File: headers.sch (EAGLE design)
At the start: 15 parts

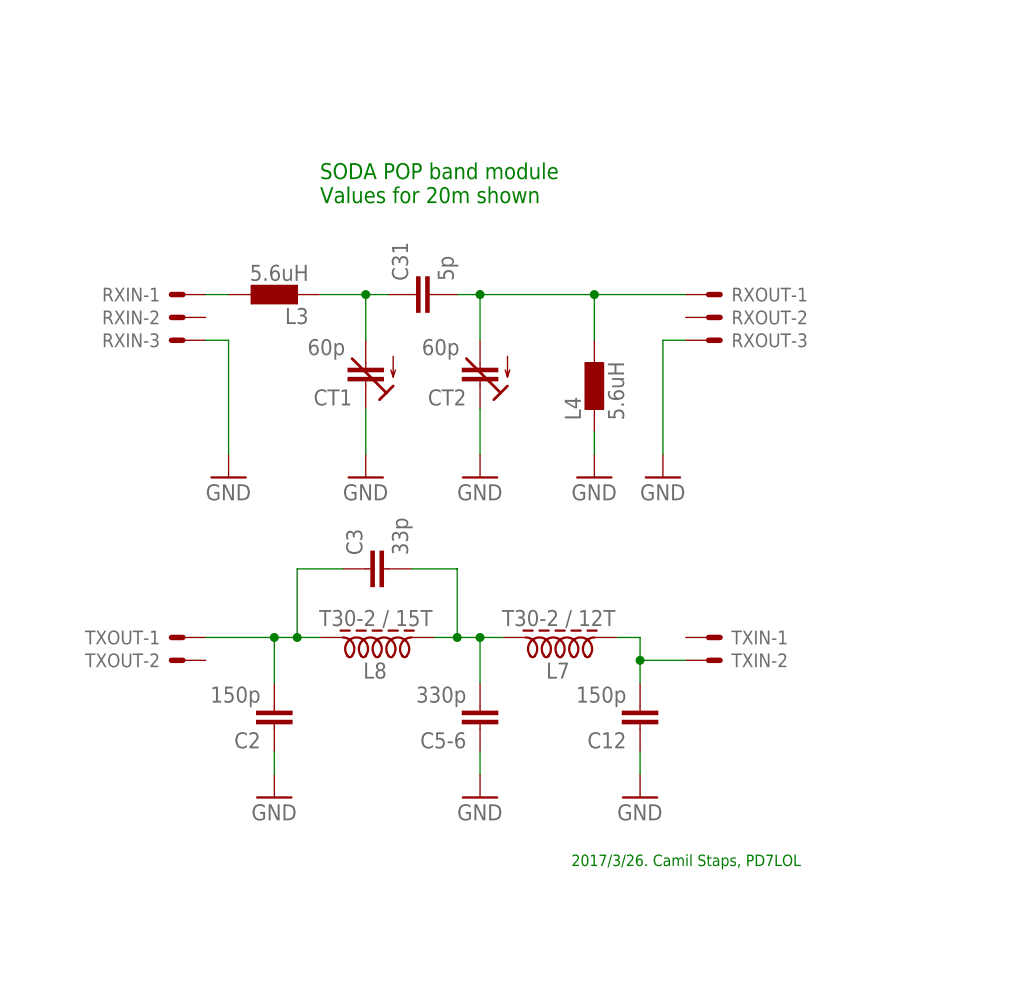
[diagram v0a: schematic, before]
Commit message: Headers: split C5-6 again, make some TX traces shorter
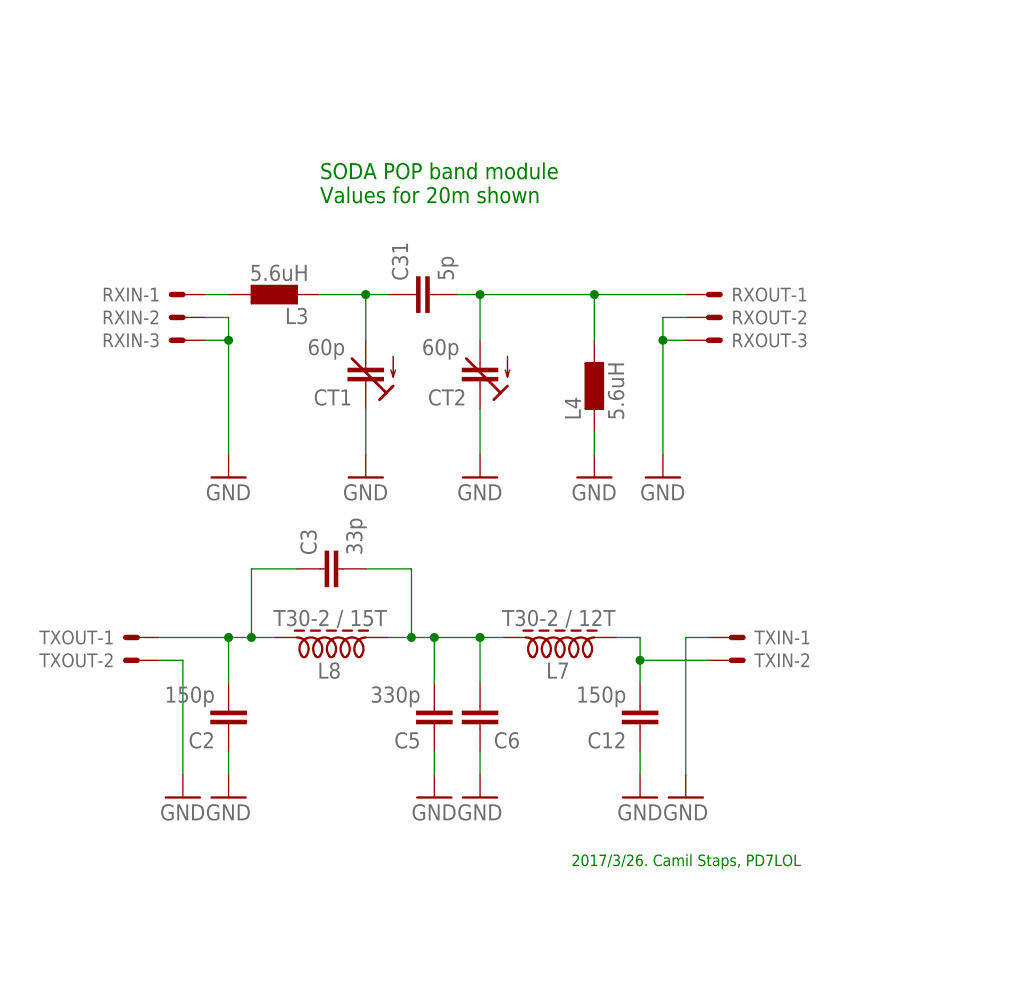
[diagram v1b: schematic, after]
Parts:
- added C5: 330p, capacitor-wima:C5/2.5
- renumbered C5-6 to C6
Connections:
- net GND: now also C5.1, RXIN-2.S, RXOUT-2.S, TXIN-1.S, TXOUT-2.S
- net N$5: now also C5.2
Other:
- moved on the sheet: C2, C3, L8, TXIN-1, TXIN-2, TXOUT-1, TXOUT-2
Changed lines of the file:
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@@
 <part name="L8" library="toroids" deviceset="INDUCTOR" device="T30-2-28AWG-15T" value="T30-2 / 15T"/>
 <part name="L7" library="toroids" deviceset="INDUCTOR" device="T30-2-28AWG-15T" value="T30-2 / 12T"/>
-<part name="C5-6" library="capacitor-wima" deviceset="C" device="5/2.5" value="330p"/>
+<part name="C5" library="capacitor-wima" deviceset="C" device="5/2.5" value="330p"/>
 <part name="C12" library="capacitor-wima" deviceset="C" device="5/2.5" value="150p"/>
 <part name="C3" library="capacitor-wima" deviceset="C" device="5/2.5" value="33p"/>
@@
 <part name="L4" library="eagle-ltspice" deviceset="L" device="0207/10" value="5.6uH"/>
 <part name="L3" library="eagle-ltspice" deviceset="L" device="0207/10" value="5.6uH"/>
+<part name="C6" library="capacitor-wima" deviceset="C" device="5/2.5" value="330p"/>
+<part name="GND9" library="supply1" deviceset="GND" device=""/>
+<part name="GND10" library="supply1" deviceset="GND" device=""/>
+<part name="GND11" library="supply1" deviceset="GND" device=""/>
 </parts>
 <sheets>
@@
 <instance part="GND4" gate="1" x="48.26" y="45.72"/>
 <instance part="GND5" gate="1" x="60.96" y="45.72"/>
-<instance part="TXIN" gate="-1" x="73.66" y="27.94" smashed="yes">
-<attribute name="NAME" x="76.2" y="27.178" size="1.524" layer="95"/>
-</instance>
-<instance part="TXIN" gate="-2" x="73.66" y="25.4"/>
-<instance part="TXOUT" gate="-1" x="15.24" y="27.94" smashed="yes" rot="MR0">
-<attribute name="NAME" x="12.7" y="27.178" size="1.524" layer="95" rot="MR0"/>
-</instance>
-<instance part="TXOUT" gate="-2" x="15.24" y="25.4" rot="MR0"/>
-<instance part="C2" gate="G$1" x="25.4" y="17.78" rot="R180"/>
-<instance part="L8" gate="G$1" x="38.1" y="27.94" smashed="yes" rot="R180">
-<attribute name="NAME" x="37.9" y="25.146" size="1.778" layer="95" rot="R180"/>
-<attribute name="VALUE" x="42.98" y="30.988" size="1.778" layer="96" rot="R180"/>
+<instance part="TXIN" gate="-1" x="76.2" y="27.94" smashed="yes">
+<attribute name="NAME" x="78.74" y="27.178" size="1.524" layer="95"/>
+</instance>
+<instance part="TXIN" gate="-2" x="76.2" y="25.4"/>
+<instance part="TXOUT" gate="-1" x="10.16" y="27.94" smashed="yes" rot="MR0">
+<attribute name="NAME" x="7.62" y="27.178" size="1.524" layer="95" rot="MR0"/>
+</instance>
+<instance part="TXOUT" gate="-2" x="10.16" y="25.4" rot="MR0"/>
+<instance part="C2" gate="G$1" x="20.32" y="17.78" rot="R180"/>
+<instance part="L8" gate="G$1" x="33.02" y="27.94" smashed="yes" rot="R180">
+<attribute name="NAME" x="32.82" y="25.146" size="1.778" layer="95" rot="R180"/>
+<attribute name="VALUE" x="37.9" y="30.988" size="1.778" layer="96" rot="R180"/>
 </instance>
 <instance part="L7" gate="G$1" x="58.42" y="27.94" smashed="yes" rot="R180">
@@
 <attribute name="VALUE" x="63.3" y="30.988" size="1.778" layer="96" rot="R180"/>
 </instance>
-<instance part="C5-6" gate="G$1" x="48.26" y="17.78" smashed="yes" rot="R180">
-<attribute name="NAME" x="46.736" y="17.399" size="1.778" layer="95" rot="R180"/>
-<attribute name="VALUE" x="46.736" y="22.479" size="1.778" layer="96" rot="R180"/>
+<instance part="C5" gate="G$1" x="43.18" y="17.78" smashed="yes" rot="R180">
+<attribute name="NAME" x="41.656" y="17.399" size="1.778" layer="95" rot="R180"/>
+<attribute name="VALUE" x="41.656" y="22.479" size="1.778" layer="96" rot="R180"/>
 </instance>
 <instance part="C12" gate="G$1" x="66.04" y="17.78" rot="R180"/>
-<instance part="C3" gate="G$1" x="35.56" y="35.56" rot="R90"/>
-<instance part="GND6" gate="1" x="25.4" y="10.16"/>
-<instance part="GND7" gate="1" x="48.26" y="10.16"/>
+<instance part="C3" gate="G$1" x="30.48" y="35.56" rot="R90"/>
+<instance part="GND6" gate="1" x="20.32" y="10.16"/>
+<instance part="GND7" gate="1" x="43.18" y="10.16"/>
 <instance part="GND8" gate="1" x="66.04" y="10.16"/>
 <instance part="L4" gate="G$1" x="60.96" y="55.88"/>
 <instance part="L3" gate="G$1" x="25.4" y="66.04" rot="R90"/>
+<instance part="C6" gate="G$1" x="48.26" y="17.78" smashed="yes" rot="R180">
+<attribute name="NAME" x="49.784" y="15.621" size="1.778" layer="95"/>
+</instance>
+<instance part="GND9" gate="1" x="48.26" y="10.16"/>
+<instance part="GND10" gate="1" x="15.24" y="10.16"/>
+<instance part="GND11" gate="1" x="71.12" y="10.16"/>
 </instances>
 <busses>
@@
 <pinref part="RXOUT" gate="-3" pin="S"/>
 <wire x1="71.12" y1="60.96" x2="68.58" y2="60.96" width="0.1524" layer="91"/>
+<pinref part="RXOUT" gate="-2" pin="S"/>
+<wire x1="71.12" y1="63.5" x2="68.58" y2="63.5" width="0.1524" layer="91"/>
+<wire x1="68.58" y1="63.5" x2="68.58" y2="60.96" width="0.1524" layer="91"/>
+<junction x="68.58" y="60.96"/>
 </segment>
 <segment>
@@
 <wire x1="17.78" y1="60.96" x2="20.32" y2="60.96" width="0.1524" layer="91"/>
 <wire x1="20.32" y1="60.96" x2="20.32" y2="48.26" width="0.1524" layer="91"/>
+<pinref part="RXIN" gate="-2" pin="S"/>
+<wire x1="17.78" y1="63.5" x2="20.32" y2="63.5" width="0.1524" layer="91"/>
+<wire x1="20.32" y1="63.5" x2="20.32" y2="60.96" width="0.1524" layer="91"/>
+<junction x="20.32" y="60.96"/>
 </segment>
 <segment>
@@
 <pinref part="C2" gate="G$1" pin="1"/>
 <pinref part="GND6" gate="1" pin="GND"/>
-<wire x1="25.4" y1="15.24" x2="25.4" y2="12.7" width="0.1524" layer="91"/>
-</segment>
-<segment>
-<pinref part="C5-6" gate="G$1" pin="1"/>
+<wire x1="20.32" y1="15.24" x2="20.32" y2="12.7" width="0.1524" layer="91"/>
+</segment>
+<segment>
+<pinref part="C5" gate="G$1" pin="1"/>
 <pinref part="GND7" gate="1" pin="GND"/>
-<wire x1="48.26" y1="15.24" x2="48.26" y2="12.7" width="0.1524" layer="91"/>
+<wire x1="43.18" y1="15.24" x2="43.18" y2="12.7" width="0.1524" layer="91"/>
 </segment>
 <segment>
@@
 <pinref part="CT2" gate="G$1" pin="E"/>
 <wire x1="48.26" y1="48.26" x2="48.26" y2="53.34" width="0.1524" layer="91"/>
+</segment>
+<segment>
+<pinref part="GND9" gate="1" pin="GND"/>
+<pinref part="C6" gate="G$1" pin="1"/>
+<wire x1="48.26" y1="12.7" x2="48.26" y2="15.24" width="0.1524" layer="91"/>
+</segment>
+<segment>
+<pinref part="TXOUT" gate="-2" pin="S"/>
+<pinref part="GND10" gate="1" pin="GND"/>
+<wire x1="12.7" y1="25.4" x2="15.24" y2="25.4" width="0.1524" layer="91"/>
+<wire x1="15.24" y1="25.4" x2="15.24" y2="12.7" width="0.1524" layer="91"/>
+</segment>
+<segment>
+<pinref part="TXIN" gate="-1" pin="S"/>
+<pinref part="GND11" gate="1" pin="GND"/>
+<wire x1="73.66" y1="27.94" x2="71.12" y2="27.94" width="0.1524" layer="91"/>
+<wire x1="71.12" y1="27.94" x2="71.12" y2="12.7" width="0.1524" layer="91"/>
 </segment>
 </net>
@@
 <net name="N$5" class="0">
 <segment>
-<pinref part="C5-6" gate="G$1" pin="2"/>
-<wire x1="45.72" y1="27.94" x2="48.26" y2="27.94" width="0.1524" layer="91"/>
-<wire x1="48.26" y1="27.94" x2="48.26" y2="22.86" width="0.1524" layer="91"/>
+<pinref part="C5" gate="G$1" pin="2"/>
+<wire x1="40.64" y1="27.94" x2="43.18" y2="27.94" width="0.1524" layer="91"/>
+<wire x1="43.18" y1="27.94" x2="43.18" y2="22.86" width="0.1524" layer="91"/>
 <pinref part="C3" gate="G$1" pin="2"/>
-<wire x1="40.64" y1="35.56" x2="45.72" y2="35.56" width="0.1524" layer="91"/>
-<wire x1="45.72" y1="35.56" x2="45.72" y2="27.94" width="0.1524" layer="91"/>
+<wire x1="35.56" y1="35.56" x2="40.64" y2="35.56" width="0.1524" layer="91"/>
+<wire x1="40.64" y1="35.56" x2="40.64" y2="27.94" width="0.1524" layer="91"/>
 <pinref part="L8" gate="G$1" pin="1"/>
-<wire x1="43.18" y1="27.94" x2="45.72" y2="27.94" width="0.1524" layer="91"/>
+<wire x1="38.1" y1="27.94" x2="40.64" y2="27.94" width="0.1524" layer="91"/>
 <pinref part="L7" gate="G$1" pin="2"/>
+<wire x1="43.18" y1="27.94" x2="48.26" y2="27.94" width="0.1524" layer="91"/>
+<junction x="40.64" y="27.94"/>
+<junction x="43.18" y="27.94"/>
+<pinref part="C6" gate="G$1" pin="2"/>
 <wire x1="48.26" y1="27.94" x2="50.8" y2="27.94" width="0.1524" layer="91"/>
-<junction x="45.72" y="27.94"/>
+<wire x1="48.26" y1="22.86" x2="48.26" y2="27.94" width="0.1524" layer="91"/>
 <junction x="48.26" y="27.94"/>
 </segment>
@@
 <wire x1="66.04" y1="27.94" x2="66.04" y2="25.4" width="0.1524" layer="91"/>
 <wire x1="66.04" y1="25.4" x2="66.04" y2="22.86" width="0.1524" layer="91"/>
-<wire x1="66.04" y1="25.4" x2="71.12" y2="25.4" width="0.1524" layer="91"/>
+<wire x1="66.04" y1="25.4" x2="73.66" y2="25.4" width="0.1524" layer="91"/>
 <junction x="66.04" y="25.4"/>
 <pinref part="L7" gate="G$1" pin="1"/>
@@
 <segment>
 <pinref part="C3" gate="G$1" pin="1"/>
-<wire x1="27.94" y1="35.56" x2="33.02" y2="35.56" width="0.1524" layer="91"/>
+<wire x1="22.86" y1="35.56" x2="27.94" y2="35.56" width="0.1524" layer="91"/>
 <pinref part="TXOUT" gate="-1" pin="S"/>
-<wire x1="17.78" y1="27.94" x2="25.4" y2="27.94" width="0.1524" layer="91"/>
+<wire x1="12.7" y1="27.94" x2="20.32" y2="27.94" width="0.1524" layer="91"/>
 <pinref part="C2" gate="G$1" pin="2"/>
-<wire x1="25.4" y1="27.94" x2="27.94" y2="27.94" width="0.1524" layer="91"/>
-<wire x1="25.4" y1="27.94" x2="25.4" y2="22.86" width="0.1524" layer="91"/>
-<wire x1="27.94" y1="35.56" x2="27.94" y2="27.94" width="0.1524" layer="91"/>
-<junction x="25.4" y="27.94"/>
+<wire x1="20.32" y1="27.94" x2="22.86" y2="27.94" width="0.1524" layer="91"/>
+<wire x1="20.32" y1="27.94" x2="20.32" y2="22.86" width="0.1524" layer="91"/>
+<wire x1="22.86" y1="35.56" x2="22.86" y2="27.94" width="0.1524" layer="91"/>
+<junction x="20.32" y="27.94"/>
 <pinref part="L8" gate="G$1" pin="2"/>
-<wire x1="27.94" y1="27.94" x2="30.48" y2="27.94" width="0.1524" layer="91"/>
-<junction x="27.94" y="27.94"/>
-</segment>
-</net>
+<wire x1="22.86" y1="27.94" x2="25.4" y2="27.94" width="0.1524" layer="91"/>
+<junction x="22.86" y="27.94"/>
+</segment>
+</net>

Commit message: SMT components on the header module
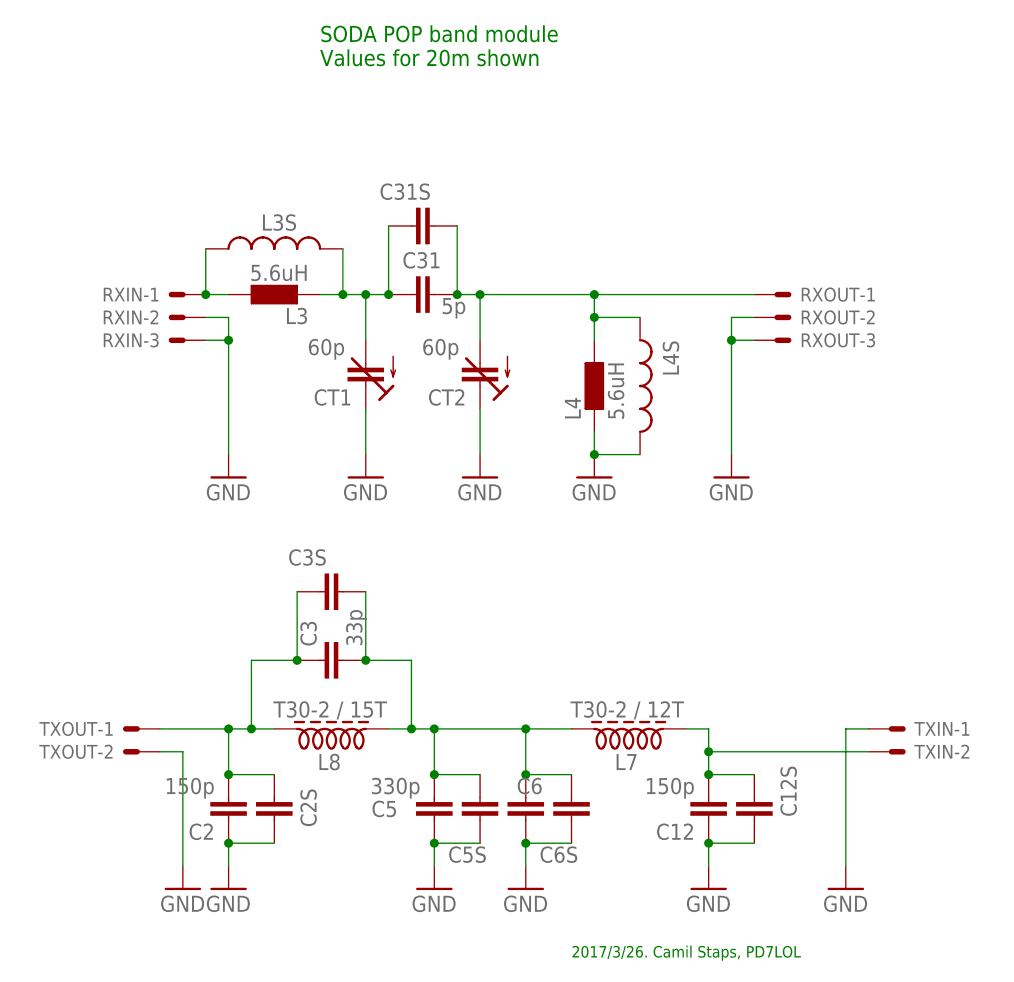
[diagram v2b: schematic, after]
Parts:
- added C12S, C2S, C31S, C3S, C5S, C6S: (no value), eagle-ltspice:CC0603
- added L3S, L4S: (no value), rcl:L-USL2012C
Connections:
- net GND: now also C12S.2, C2S.2, C5S.2, C6S.2, L4S.2
- net N$1: now also L3S.1
- net N$2: now also C31S.1, L3S.2
- net N$4: now also C31S.2, L4S.1
- net N$5: now also C3S.2, C5S.1, C6S.1
- net N$6: now also C12S.1
- net N$8: now also C2S.1, C3S.1
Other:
- moved on the sheet: C12, C2, C3, C5, C6, L7, L8, RXOUT-1, RXOUT-2, RXOUT-3, TXIN-1, TXIN-2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
